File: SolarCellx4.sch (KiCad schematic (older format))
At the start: 0 parts

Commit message: finish
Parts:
- added C? (x8): 1n, symbol Device:C
- added C? (x8): 100u, symbol Main-rescue:C-Device
- added L? (x4): 10uH, symbol Main-rescue:L-Device
- added R? (x4): 330k, symbol Device:R
- added R? (x4): 768k, symbol Device:R
- added R? (x4): 1k, symbol Main-rescue:R-Device
- added SC? (x4): Solar_Cell, symbol Device:Solar_Cell
- added U? (x4): SPV1040, symbol Main-rescue:SPV1040-CustomSymbols
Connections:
- net OUT+: now also C?.1, C?.1, C?.1, C?.1, R?.1, R?.1, R?.1, R?.1, U?.4 (VOUT), U?.4 (VOUT), U?.4 (VOUT), U?.4 (VOUT), U?.6 (ICTRL-), U?.6 (ICTRL-), U?.6 (ICTRL-), U?.6 (ICTRL-), U?.7 (ICTRL+), U?.7 (ICTRL+), U?.7 (ICTRL+), U?.7 (ICTRL+)
- net OUT-: now also C?.2, C?.2, C?.2, C?.2, C?.2, C?.2, C?.2, C?.2, C?.2, C?.2, C?.2, C?.2, C?.2, C?.2, C?.2, C?.2, R?.2, R?.2, R?.2, R?.2, SC?.2 (-), SC?.2 (-), SC?.2 (-), SC?.2 (-), U?.2 (GND), U?.2 (GND), U?.2 (GND), U?.2 (GND)
- new net: C?.1, L?.1, R?.2, SC?.1 (+) (x4)
- new net: C?.1, R?.1, R?.2, U?.5 (VCTRL) (x4)
- new net: C?.1, R?.1, U?.1 (MPP-SET), U?.8 (XSHUT) (x4)
- new net: L?.2, U?.3 (LX) (x4)
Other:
- note added: "Inductor:\nB82442T1103K050"

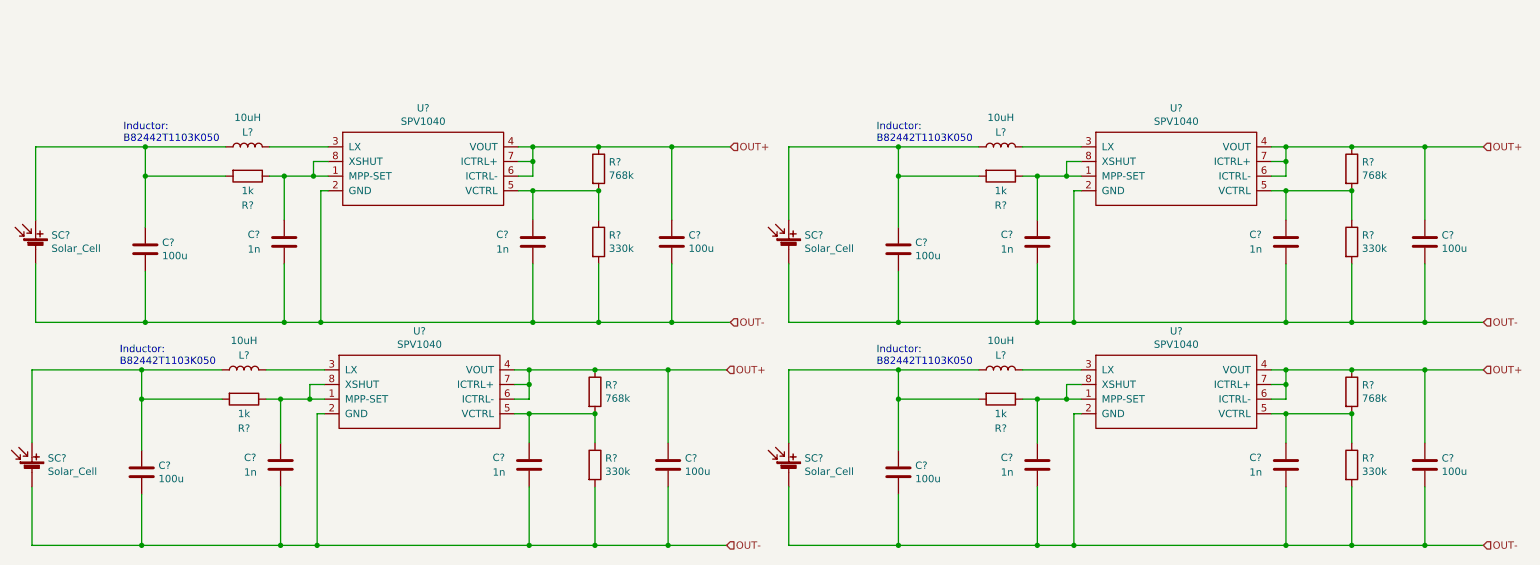
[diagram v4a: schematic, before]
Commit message: added burn wire load switches
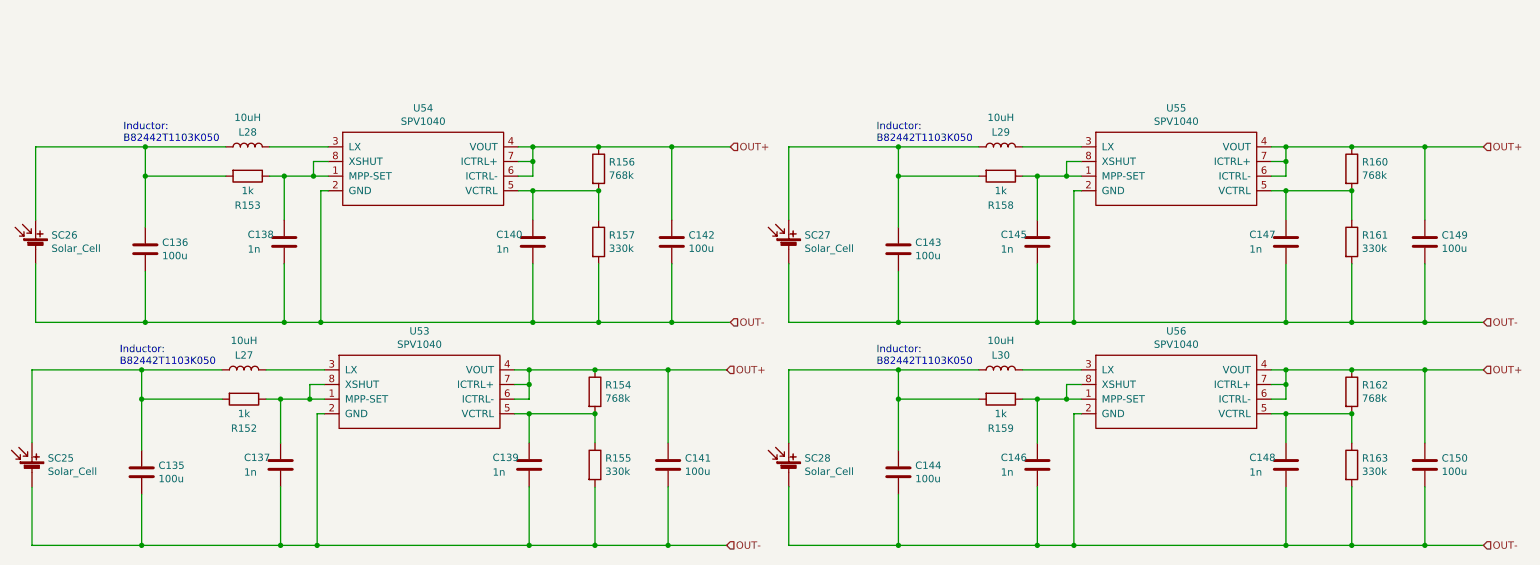
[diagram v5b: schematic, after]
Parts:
- gave numbers to parts that had none: 40
